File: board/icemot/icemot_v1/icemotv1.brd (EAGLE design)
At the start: 160 x 100 mm, 79 parts, among them U1 ICE40HX4K, U2 EFM32WG332FXXX-QFP64, U3 MAX5723/4/5, U4 TLV4379, X1 MSTBV4, Y1 48MHz

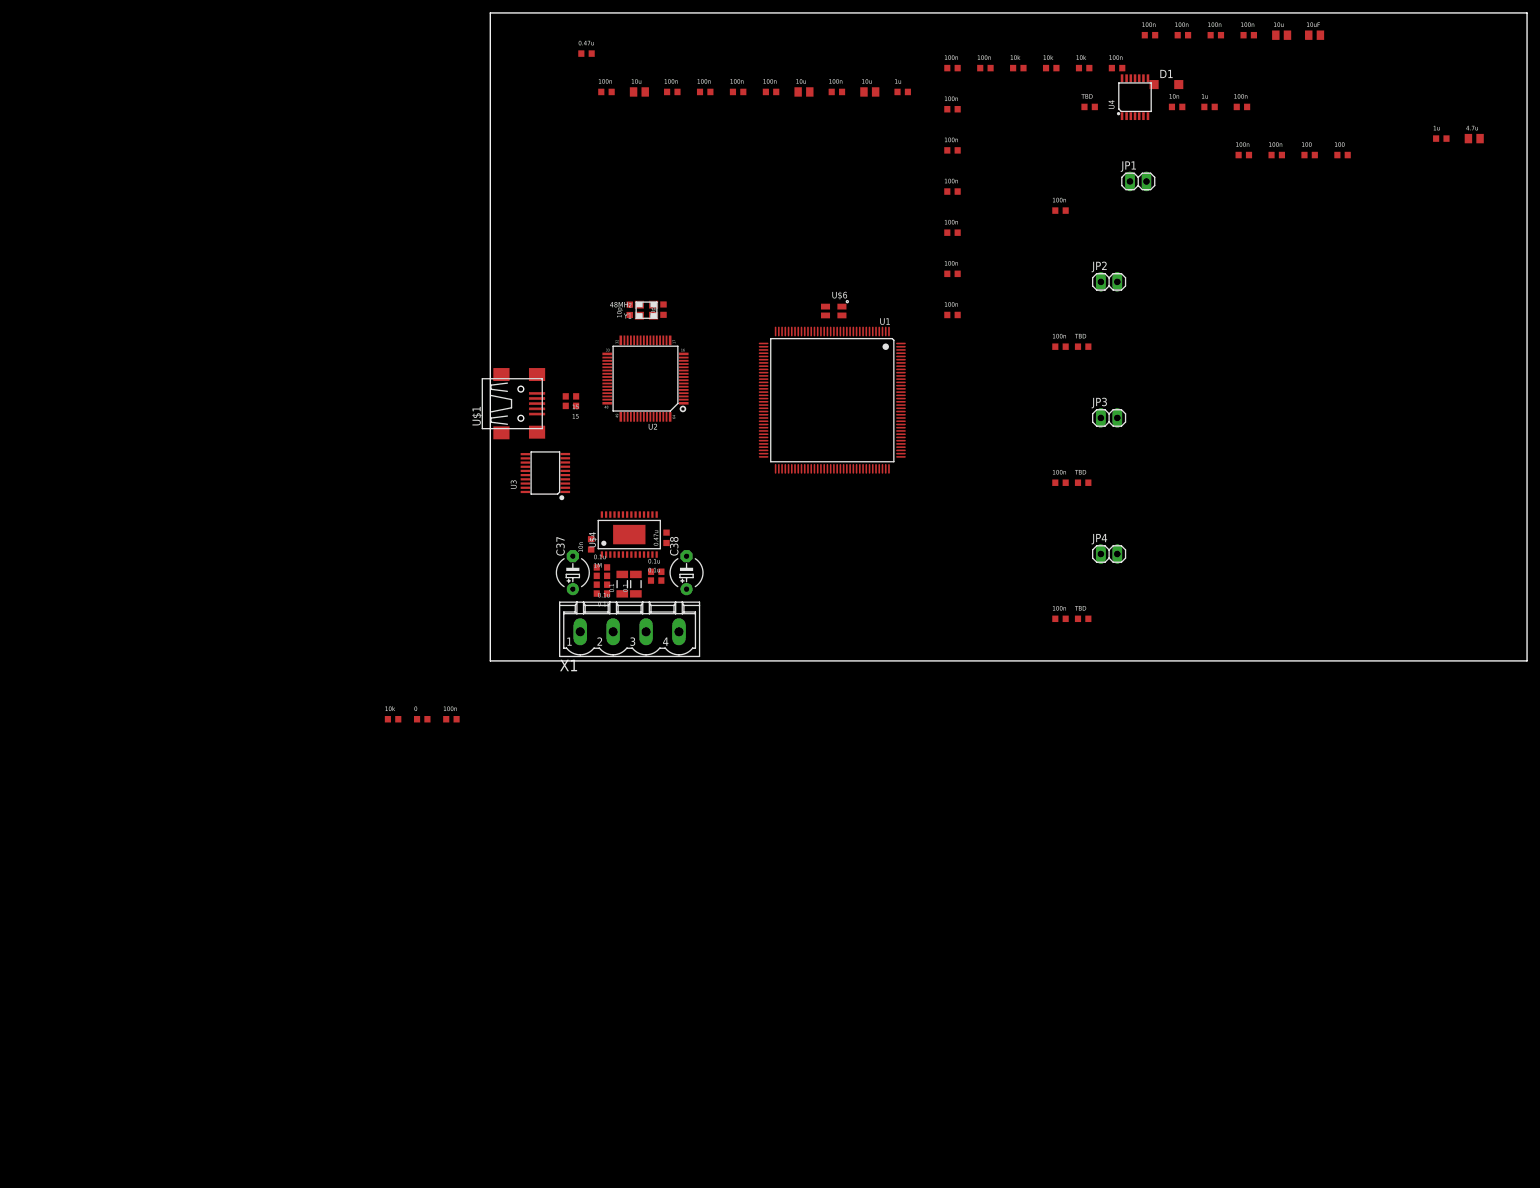
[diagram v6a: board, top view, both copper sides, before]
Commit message: remove ICE40 and EFM32, add a S6 LX9
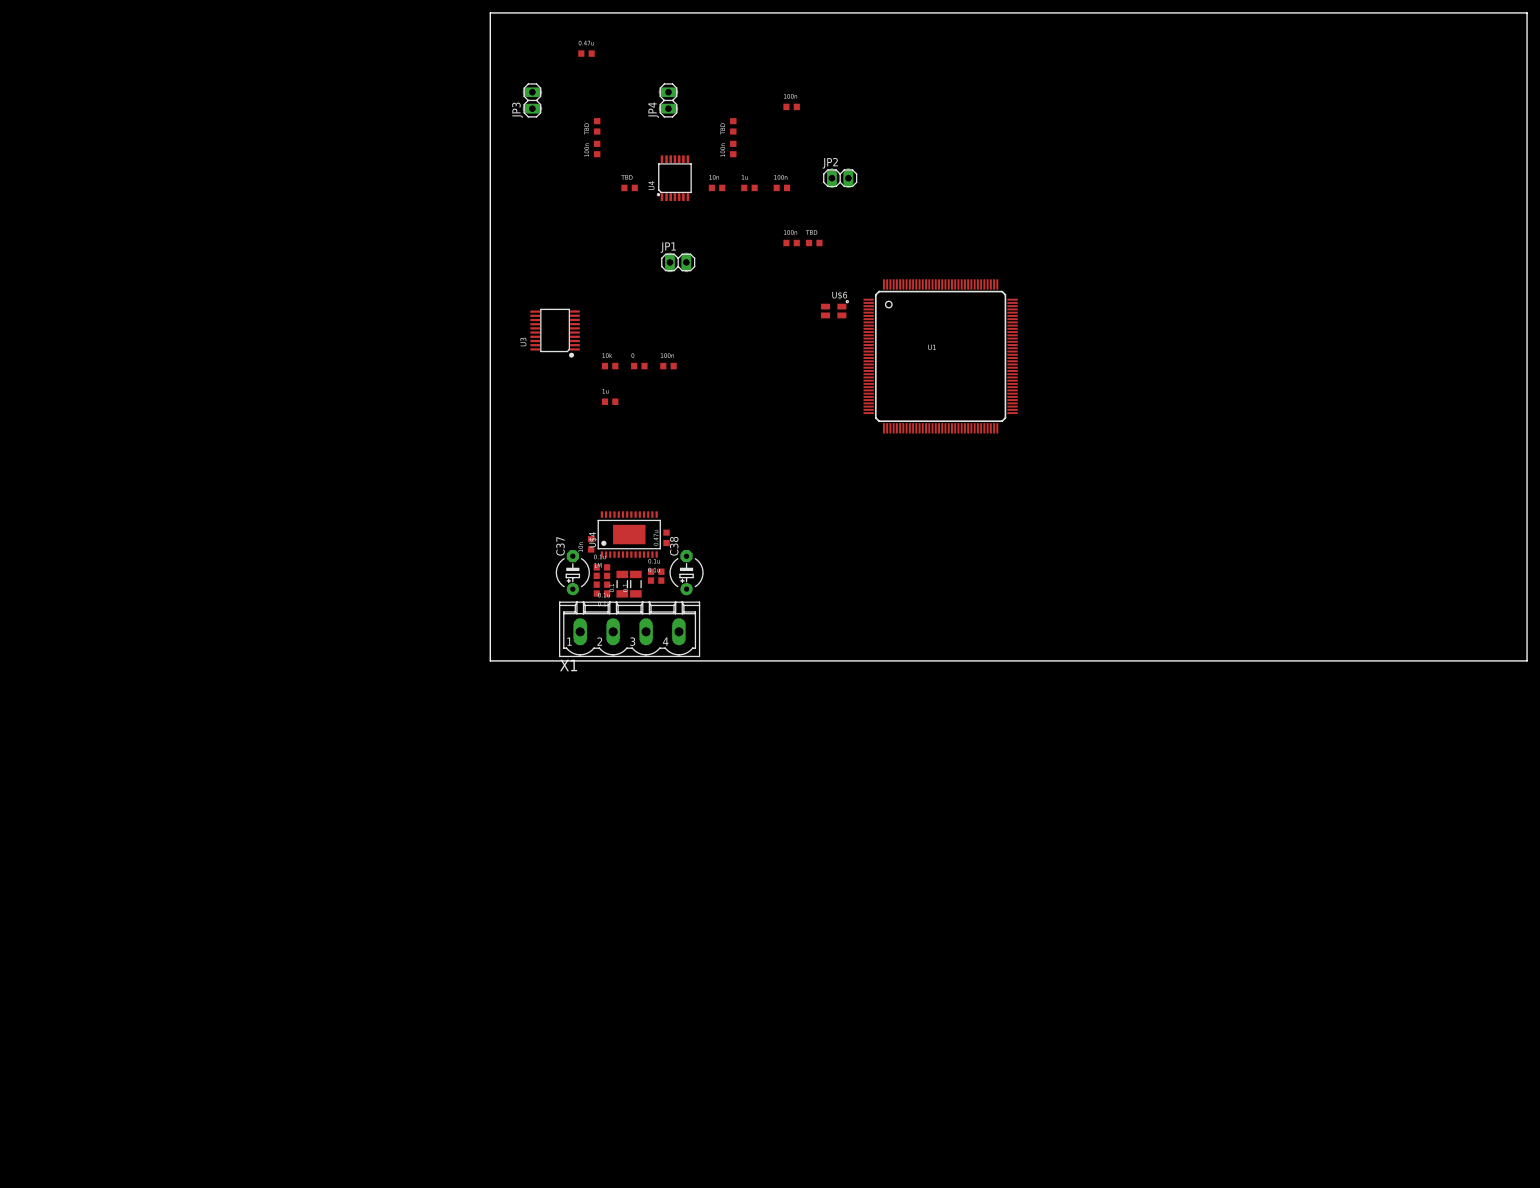
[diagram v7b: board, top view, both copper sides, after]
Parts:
- removed C10, C15, C16, C19, C20, C21, C22, C23, C24, C25, C26, C27, C28, C29, C3, C30, C31, C5, C6, C7, C8: 100n, standard_passive:R0603
- removed C11: 4.7u, standard_passive:R0805
- removed C12: 1u, standard_passive:R0603
- removed C13, C14: 10p, standard_passive:R0603
- removed C17: 10uF, standard_passive:R0805
- removed C18, C2, C4, C9: 10u, standard_passive:R0805
- removed D1: (no value), diode:SOD123
- removed R1, R2: 15, standard_passive:R0603
- removed R3, R4: 100, standard_passive:R0603
- removed R5, R6, R7: 10k, standard_passive:R0603
- removed U$1: USB-SHIELD, usb-header:USB-M-S1
- removed U2: EFM32WG332FXXX-QFP64, EFM32:TQFP64-0.5-12X12MM
- removed Y1: 48MHz, xtals:3.2X2.5MM
- U1: value ICE40HX4K -> 6SLX9TQG144; device ICE40HX:TQFP144 -> xilinx:TQ144
- moved JP3 101.6 mm to (6.50, 86.5), turned to 90 degrees
- moved JP4 97.6 mm to (27.5, 86.5), turned to 90 degrees
- moved R14 93.2 mm to (37.5, 82.5), turned to 90 degrees
- moved R13 93.0 mm to (16.5, 82.5), turned to 90 degrees
- moved C45 88.4 mm to (37.5, 79.0), turned to 90 degrees
- moved C44 88.1 mm to (16.5, 79.0), turned to 90 degrees
- moved C39 72.1 mm to (45.0, 73.0)
- moved C40 72.1 mm to (40.0, 73.0)
- moved C41 72.1 mm to (35.0, 73.0)
- moved JP1 72.1 mm to (29.0, 61.5)
- moved R11 72.1 mm to (21.5, 73.0)
- moved U4 72.1 mm to (28.5, 74.5)
- moved C1 65.8 mm to (18.5, 40.0)
- moved C49 64.0 mm to (27.5, 45.5)
- moved R15 64.0 mm to (23.0, 45.5)
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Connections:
- removed net +1V2: C19.1, C20.1, C21.1, C22.1, R3.1, R4.1, U1.111, U1.27, U1.40, U1.92
- removed net CDONE: R6.1, U1.65
- removed net CONF_CS: R5.2, U1.71, U2.62
- removed net CRESET: R7.1, U1.66
- removed net N$1: C1.1, U2.40
- removed net N$10: C16.1, C18.1, R4.2, U1.54
- removed net N$11: C15.1, C17.1, R3.2, U1.126
- removed net N$12: C15.2, C17.2, U1.127
- removed net N$13: C16.2, C18.2, U1.53
- removed net N$14: D1.C, U1.108
- removed net N$15: U2.64
- removed net N$2: R1.1, U2.47
- removed net N$21: U$6.3, U1.21
- removed net N$3: R1.2, U$1.D-
- removed net N$4: C11.1, U$1.VBUS, U2.45, U2.52
- removed net N$5: C12.2, U2.46
- removed net N$6: R2.2, U$1.D+
- removed net N$7: R2.1, U2.48
- removed net N$8: C13.1, U2.25, Y1.3
- removed net N$9: C14.1, U2.24, Y1.1
- removed net VCCIO0: U1.123, U1.131
- removed net VCCIO1: U1.100, U1.89
- removed net VCCIO3: U1.30, U1.6
- removed net VPP_FAST: U1.109
- net +3V3: now also C1.1; no longer C10.2, C2.1, C23.1, C24.1, C25.1, C26.1, C27.1, C28.1, C29.1, C3.1, C30.1, C31.1, C4.1, C5.1, C6.1, C7.1, C8.1, C9.1, D1.A, R6.2, R7.2, U1.46, U1.57, U1.72, U2.23, U2.26, U2.27, U2.39, U2.55, U2.7
- net CONF_MISO: no longer U1.67, U2.60
- net CONF_MOSI: no longer U1.68, U2.59
- net CONF_SCK: no longer U1.70, U2.61
- net DAC_CS: no longer U2.63
- net GND: now also U1.P108, U1.P113, U1.P13, U1.P130, U1.P136, U1.P25, U1.P3, U1.P49, U1.P54, U1.P68, U1.P77, U1.P91, U1.P96; no longer C10.1, C11.2, C12.1, C13.2, C14.2, C19.2, C2.2, C20.2, C21.2, C22.2, C23.2, C24.2, C25.2, C26.2, C27.2, C28.2, C29.2, C3.2, C30.2, C31.2, C4.2, C5.2, C6.2, C7.2, C8.2, C9.2, R5.1, U$1.GND, U$1.GND@1, U$1.GND@2, U$1.GND@3, U$1.GND@4, U1.103, U1.13, U1.132, U1.14, U1.140, U1.5, U1.59, U1.69, U1.86, U2.22, U2.56, U2.8
- net MOT1_DIR: no longer U1.60
- net MOT1_EN: no longer U1.61
- net MOT1_FAULT: no longer U1.62
- net MOT1_RST: no longer U1.55
- net MOT1_STEP: no longer U1.56
- net T1_AMP: no longer U2.31
- net T2_AMP: no longer U2.32
- net T3_AMP: no longer U2.33
- net T4_AMP: no longer U2.34

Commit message: added ADC DCDC and copied 5 drv8825
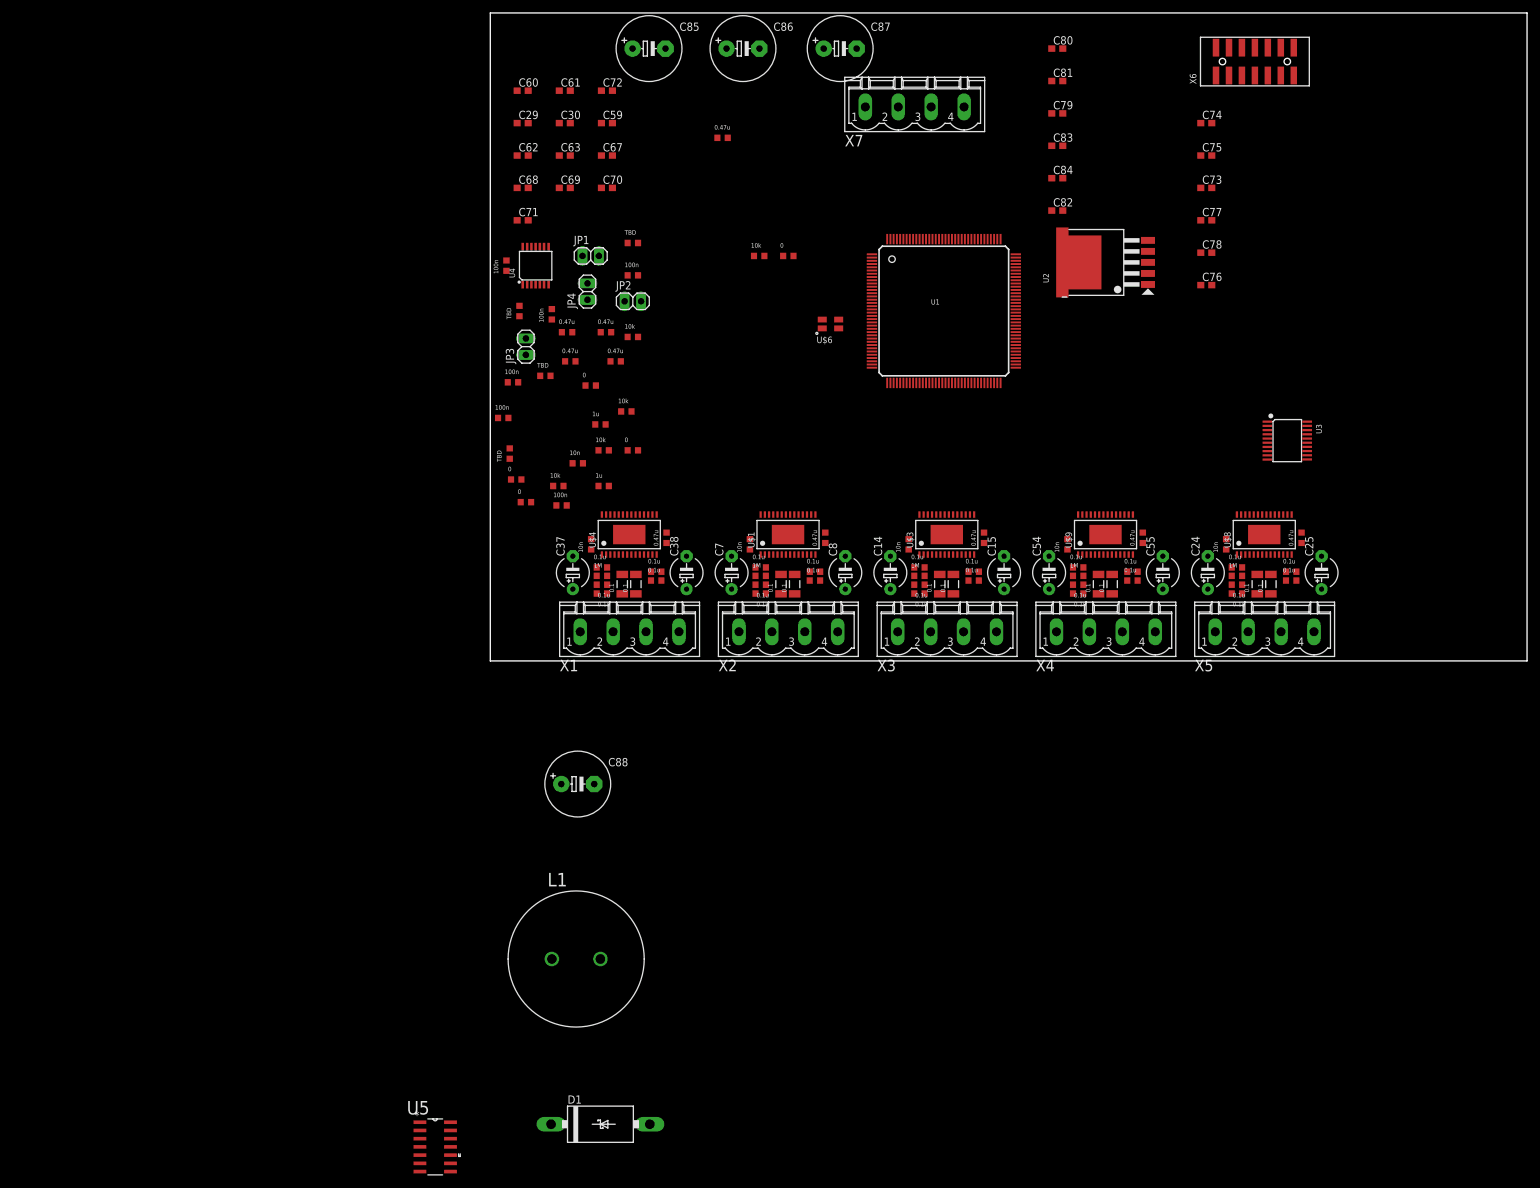
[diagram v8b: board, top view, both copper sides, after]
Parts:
- added C10, C12, C13, C17, C18, C20, C22, C23, C27, C28, C3, C5, C50, C52, C53, C57, C58, C6, C65, C66: 0.1u, standard_passive:R0603
- added C11, C16, C21, C26, C4, C51, C56, C64: 0.47u, standard_passive:R0603
- added C14, C15, C24, C25, C54, C55, C7, C8: (no value), rcl:E5-5
- added C19, C2, C31, C9: 10n, standard_passive:R0603
- added C29, C30, C59, C62, C63, C67, C68, C69, C70, C71, C73, C76, C79, C82: 4.7u, rcl:C0603
- added C60, C61, C72, C74, C75, C77, C78, C80, C81, C83, C84: 470n, rcl:C0603
- added C85, C86, C87, C88: (no value), rcl:E5-10,5
- added D1: MBR360G, diode:DO201T15
- added L1: 100UH, Panasonic-ELC:IND_ELC18B
- added R1, R19, R2, R24, R25, R4, R5, R7: 0.1, standard_passive:R1206
- added R17, R22, R27, R32: 0, standard_passive:R0603
- added R18, R23, R28, R33: 10k, standard_passive:R0603
- added R20, R26, R3, R6: 1M, standard_passive:R0603
- added U$1, U$3, U$8, U$9: DRV8825PWP, motor_drivers:TSSOP-28
- added U2: LM2576HVS-5.0/NOPB-TO263-5, Seeed-OPL-ic:TO-263-5
- added U5: MCP3204-CI/SL, mcp3204:SOIC127P600X175-14N
- added X2, X3, X4, X5, X7: MSTBV4, con-phoenix-508:MSTBV4
- added X6: 87832-14, con-molex:87832-14
- moved U3 114.3 mm to (123.0, 34.0), turned to 270 degrees
- moved R14 61.2 mm to (3.00, 32.0)
- moved C39 55.8 mm to (2.00, 37.5)
- moved C43 48.1 mm to (3.50, 43.0)
- moved C41 47.6 mm to (13.5, 30.5)
- moved R12 46.3 mm to (8.50, 44.0)
- moved C40 43.1 mm to (17.0, 36.5)
- moved C34 43.1 mm to (11.8, 50.7)
- moved C45 39.4 mm to (2.50, 61.0)
- moved JP3 38.0 mm to (5.50, 48.5)
- moved JP2 37.2 mm to (22.0, 55.5)
- moved C42 35.7 mm to (22.0, 59.5)
- moved JP4 32.0 mm to (15.0, 57.0)
- moved R13 30.9 mm to (4.50, 54.0)
- moved C49 27.1 mm to (11.0, 24.0)
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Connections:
- removed net +40V1: C47.1, C48.1
- removed net N$34: U3.3
- removed net N$35: U3.4
- removed net N$36: U3.5
- new net +1V2: C29.1, C30.1, C59.1, C60.1, C61.1
- new net +5V: C88.+, L1.1, U2.4
- new net MOT2_DIR: U$1.20
- new net MOT2_EN: U$1.21
- new net MOT2_FAULT: R18.1, U$1.18
- new net MOT2_RST: U$1.16, U$1.17
- new net MOT2_STEP: U$1.22
- new net MOT2_VREF: C16.1, U$1.12, U$1.13, U3.3
- new net MOT3_DIR: U$3.20
- new net MOT3_EN: U$3.21
- new net MOT3_FAULT: R23.1, U$3.18
- new net MOT3_RST: U$3.16, U$3.17
- new net MOT3_STEP: U$3.22
- new net MOT3_VREF: C26.1, U$3.12, U$3.13, U3.4
- new net MOT4_DIR: U$9.20
- new net MOT4_EN: U$9.21
- new net MOT4_FAULT: R28.1, U$9.18
- new net MOT4_RST: U$9.16, U$9.17
- new net MOT4_STEP: U$9.22
- new net MOT4_VREF: C56.1, U$9.12, U$9.13, U3.5
- new net MOT5_DIR: U$8.20
- new net MOT5_EN: U$8.21
- new net MOT5_FAULT: R33.1, U$8.18
- new net MOT5_RST: U$8.16, U$8.17
- new net MOT5_STEP: U$8.22
- new net MOT5_VREF: C64.1, U$8.12, U$8.13, U3.6
- new net N$1: R2.2, U$1.6
- new net N$10: R17.2, U$1.19
- new net N$11: R5.2, U$3.6
- new net N$12: R4.2, U$3.9
- new net N$13: C9.1, U$3.1
- new net N$14: C9.2, U$3.2
- new net N$15: C10.1, R6.1, U$3.3
- new net N$2: R1.2, U$1.9
- new net N$21: U$3.5, X3.1
- new net N$22: U$3.7, X3.2
- new net N$23: U$3.8, X3.3
- new net N$25: U$3.10, X3.4
- new net N$26: R22.2, U$3.19
- new net N$27: R25.2, U$9.6
- new net N$28: R24.2, U$9.9
- new net N$3: C2.1, U$1.1
- new net N$33: C31.1, U$9.1
- new net N$4: C2.2, U$1.2
- new net N$41: C31.2, U$9.2
- new net N$42: C50.1, R26.1, U$9.3
- new net N$43: U$9.5, X4.1
- new net N$44: U$9.7, X4.2
- new net N$45: U$9.8, X4.3
- new net N$46: U$9.10, X4.4
- new net N$47: R27.2, U$9.19
- new net N$48: R19.2, U$8.6
- new net N$49: R7.2, U$8.9
- new net N$5: C3.1, R3.1, U$1.3
- new net N$50: C19.1, U$8.1
- new net N$51: C19.2, U$8.2
- new net N$52: C20.1, R20.1, U$8.3
- new net N$53: U$8.5, X5.1
- new net N$54: U$8.7, X5.2
- new net N$55: U$8.8, X5.3
- new net N$56: U$8.10, X5.4
- new net N$57: R32.2, U$8.19
- new net N$58: U$6.3, U1.P21
- new net N$6: U$1.5, X2.1
- new net N$7: U$1.7, X2.2
- new net N$8: U$1.8, X2.3
- new net N$9: U$1.10, X2.4
- new net TCK: U1.P109, X6.6
- new net TDI: U1.P110, X6.10
- new net TDO: U1.P106, X6.8
- new net TMS: U1.P107, X6.4
- new net VDD: U5.14
- net +3V3: now also C11.2, C21.2, C4.2, C51.2, C62.1, C63.1, C67.1, C68.1, C69.1, C70.1, C71.1, C72.1, C73.1, C74.1, C75.1, C76.1, C77.1, C78.1, C79.1, C80.1, C81.1, C82.1, C83.1, C84.1, R17.1, R18.2, R22.1, R23.2, R27.1, R28.2, R32.1, R33.2, U$1.15, U$1.24, U$1.25, U$1.26, U$3.15, U$3.24, U$3.25, U$3.26, U$8.15, U$8.24, U$8.25, U$8.26, U$9.15, U$9.24, U$9.25, U$9.26, U1.P129, U1.P20, U1.P36, U1.P53, U1.P90, X6.2
- net +40V: now also C10.2, C12.1, C13.1, C14.+, C15.+, C17.1, C18.1, C20.2, C22.1, C23.1, C24.+, C25.+, C27.1, C28.1, C3.2, C47.1, C48.1, C5.1, C50.2, C52.1, C53.1, C54.+, C55.+, C57.1, C58.1, C6.1, C65.1, C66.1, C7.+, C8.+, C85.+, C86.+, C87.+, R20.2, R26.2, R3.2, R6.2, U$1.11, U$1.4, U$3.11, U$3.4, U$8.11, U$8.4, U$9.11, U$9.4, U2.1, X7.1, X7.2
- net GND: now also C11.1, C12.2, C13.2, C14.-, C15.-, C16.2, C17.2, C18.2, C21.1, C22.2, C23.2, C24.-, C25.-, C26.2, C27.2, C28.2, C29.2, C30.2, C4.1, C5.2, C51.1, C52.2, C53.2, C54.-, C55.-, C56.2, C57.2, C58.2, C59.2, C6.2, C60.2, C61.2, C62.2, C63.2, C64.2, C65.2, C66.2, C67.2, C68.2, C69.2, C7.-, C70.2, C71.2, C72.2, C73.2, C74.2, C75.2, C76.2, C77.2, C78.2, C79.2, C8.-, C80.2, C81.2, C82.2, C83.2, C84.2, C85.-, C86.-, C87.-, C88.-, D1.A, R1.1, R19.1, R2.1, R24.1, R25.1, R4.1, R5.1, R7.1, U$1.14, U$1.28, U$1.29, U$3.14, U$3.28, U$3.29, U$8.14, U$8.28, U$8.29, U$9.14, U$9.28, U$9.29, U1.P73, U2.3, U2.5, U2.PAD, U5.12, U5.7, X6.11, X6.13, X6.3, X6.5, X6.7, X6.9, X7.3, X7.4
- net N$37: now also D1.C, L1.2, U2.2; no longer U3.6
